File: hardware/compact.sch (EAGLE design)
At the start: 26 parts, among them SW1 SWITCH_SPDT, U1 MCP73831, U2 EDISON_CONNECTOR_FULLMOUNTING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, U3 EDISON_CONNECTOR_FULLHEADER

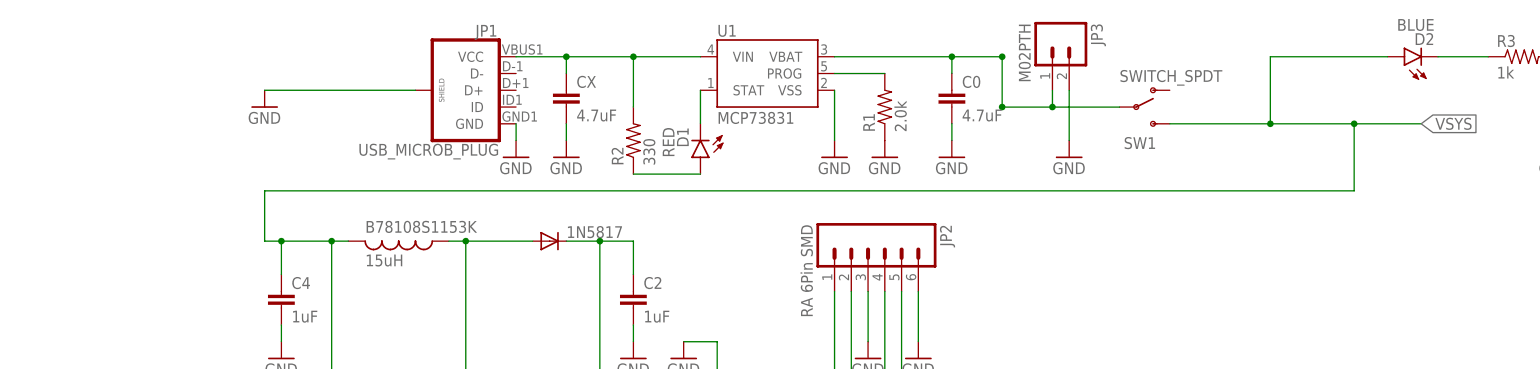
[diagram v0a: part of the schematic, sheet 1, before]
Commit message: add USB data lines, use 1.8v line, not vcc, for Max3218, DRC fixes
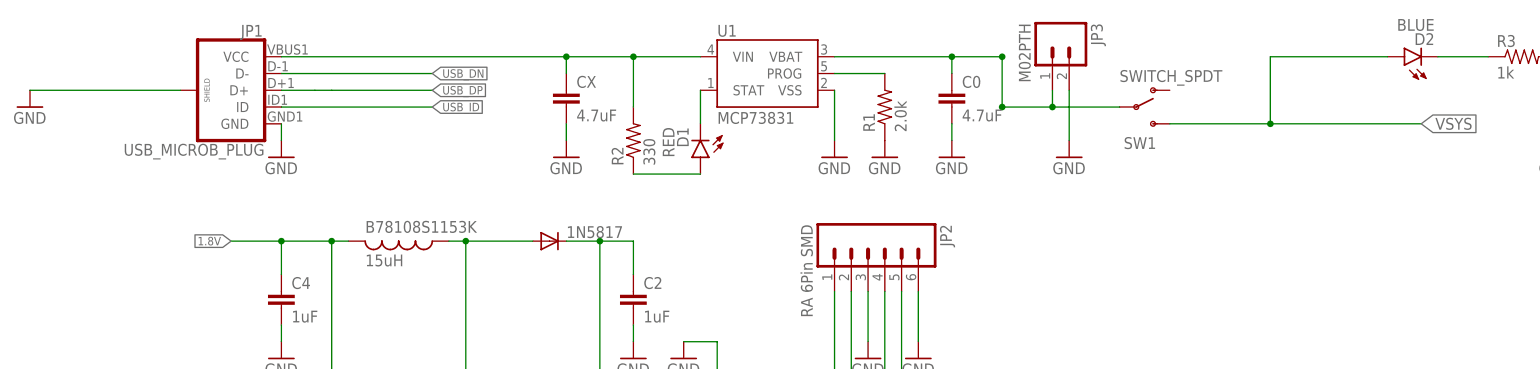
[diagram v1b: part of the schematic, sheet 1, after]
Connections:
- net 1.8V: now also B78108S1153K.2, C4.1, MAX3218.4, MAX3218.6
- net USB_DN: now also JP1.D-
- net USB_DP: now also JP1.D+
- net USB_ID: now also JP1.ID
- net VSYS: no longer B78108S1153K.2, C4.1, MAX3218.4, MAX3218.6
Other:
- moved on the sheet: JP1
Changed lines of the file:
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@@
 <instance part="FID1" gate="G$1" x="246.38" y="25.4"/>
 <instance part="FID2" gate="G$1" x="241.3" y="25.4"/>
-<instance part="JP1" gate="G$1" x="66.04" y="172.72" rot="MR0"/>
-<instance part="GND1" gate="1" x="73.66" y="162.56"/>
-<instance part="GND2" gate="1" x="35.56" y="170.18"/>
+<instance part="JP1" gate="G$1" x="30.48" y="172.72" rot="MR0"/>
+<instance part="GND1" gate="1" x="38.1" y="162.56"/>
+<instance part="GND2" gate="1" x="0" y="170.18"/>
 <instance part="CX" gate="G$1" x="81.28" y="170.18"/>
 <instance part="SW1" gate="G$1" x="167.64" y="170.18"/>
@@
 <pinref part="GND2" gate="1" pin="GND"/>
 <pinref part="JP1" gate="G$1" pin="SHIELD"/>
-<wire x1="35.56" y1="172.72" x2="58.42" y2="172.72" width="0.1524" layer="91"/>
+<wire x1="0" y1="172.72" x2="22.86" y2="172.72" width="0.1524" layer="91"/>
 </segment>
 <segment>
 <pinref part="JP1" gate="G$1" pin="GND"/>
 <pinref part="GND1" gate="1" pin="GND"/>
-<wire x1="73.66" y1="167.64" x2="73.66" y2="165.1" width="0.1524" layer="91"/>
+<wire x1="38.1" y1="167.64" x2="38.1" y2="165.1" width="0.1524" layer="91"/>
 </segment>
 <segment>
@@
 <pinref part="JP1" gate="G$1" pin="VCC"/>
 <pinref part="U1" gate="G$1" pin="VIN"/>
-<wire x1="73.66" y1="177.8" x2="81.28" y2="177.8" width="0.1524" layer="91"/>
+<wire x1="38.1" y1="177.8" x2="81.28" y2="177.8" width="0.1524" layer="91"/>
 <pinref part="CX" gate="G$1" pin="1"/>
 <wire x1="81.28" y1="177.8" x2="91.44" y2="177.8" width="0.1524" layer="91"/>
@@
 <wire x1="172.72" y1="167.64" x2="187.96" y2="167.64" width="0.1524" layer="91"/>
 <label x="210.82" y="167.64" size="1.778" layer="95" xref="yes"/>
-<wire x1="187.96" y1="167.64" x2="200.66" y2="167.64" width="0.1524" layer="91"/>
-<wire x1="200.66" y1="167.64" x2="210.82" y2="167.64" width="0.1524" layer="91"/>
+<wire x1="187.96" y1="167.64" x2="210.82" y2="167.64" width="0.1524" layer="91"/>
 <wire x1="187.96" y1="177.8" x2="187.96" y2="167.64" width="0.1524" layer="91"/>
 <junction x="187.96" y="167.64"/>
-<junction x="200.66" y="167.64"/>
-<wire x1="200.66" y1="167.64" x2="200.66" y2="157.48" width="0.1524" layer="91"/>
-<wire x1="200.66" y1="157.48" x2="35.56" y2="157.48" width="0.1524" layer="91"/>
-<wire x1="35.56" y1="157.48" x2="35.56" y2="149.86" width="0.1524" layer="91"/>
-<wire x1="35.56" y1="149.86" x2="38.1" y2="149.86" width="0.1524" layer="91"/>
-<junction x="38.1" y="149.86"/>
-<wire x1="38.1" y1="149.86" x2="38.1" y2="144.78" width="0.1524" layer="91"/>
-<wire x1="38.1" y1="149.86" x2="45.72" y2="149.86" width="0.1524" layer="91"/>
-<junction x="45.72" y="149.86"/>
-<pinref part="C4" gate="G$1" pin="1"/>
-<pinref part="MAX3218" gate="G$1" pin="6"/>
-<wire x1="58.42" y1="111.76" x2="45.72" y2="111.76" width="0.1524" layer="91"/>
-<wire x1="45.72" y1="111.76" x2="45.72" y2="116.84" width="0.1524" layer="91"/>
-<pinref part="B78108S1153K" gate="G$1" pin="2"/>
-<wire x1="45.72" y1="116.84" x2="45.72" y2="149.86" width="0.1524" layer="91"/>
-<wire x1="48.26" y1="149.86" x2="45.72" y2="149.86" width="0.1524" layer="91"/>
-<junction x="45.72" y="116.84"/>
-<pinref part="MAX3218" gate="G$1" pin="4"/>
-<wire x1="58.42" y1="116.84" x2="45.72" y2="116.84" width="0.1524" layer="91"/>
 <pinref part="D2" gate="G$1" pin="A"/>
 <wire x1="187.96" y1="177.8" x2="205.74" y2="177.8" width="0.1524" layer="91"/>
@@
 </segment>
 </net>
+<net name="1.8V" class="0">
+<segment>
+<label x="30.48" y="149.86" size="1.27" layer="95" rot="R180" xref="yes"/>
+<pinref part="C4" gate="G$1" pin="1"/>
+<junction x="38.1" y="149.86"/>
+<wire x1="38.1" y1="149.86" x2="38.1" y2="144.78" width="0.1524" layer="91"/>
+<wire x1="38.1" y1="149.86" x2="45.72" y2="149.86" width="0.1524" layer="91"/>
+<junction x="45.72" y="149.86"/>
+<pinref part="B78108S1153K" gate="G$1" pin="2"/>
+<wire x1="48.26" y1="149.86" x2="45.72" y2="149.86" width="0.1524" layer="91"/>
+<wire x1="45.72" y1="116.84" x2="45.72" y2="149.86" width="0.1524" layer="91"/>
+<junction x="45.72" y="116.84"/>
+<pinref part="MAX3218" gate="G$1" pin="4"/>
+<wire x1="58.42" y1="116.84" x2="45.72" y2="116.84" width="0.1524" layer="91"/>
+<pinref part="MAX3218" gate="G$1" pin="6"/>
+<wire x1="58.42" y1="111.76" x2="45.72" y2="111.76" width="0.1524" layer="91"/>
+<wire x1="45.72" y1="111.76" x2="45.72" y2="116.84" width="0.1524" layer="91"/>
+<wire x1="30.48" y1="149.86" x2="38.1" y2="149.86" width="0.1524" layer="91"/>
+</segment>
+</net>
+<net name="USB_DN" class="0">
+<segment>
+<label x="60.96" y="175.26" size="1.27" layer="95" xref="yes"/>
+<pinref part="JP1" gate="G$1" pin="D-"/>
+<wire x1="60.96" y1="175.26" x2="38.1" y2="175.26" width="0.1524" layer="91"/>
+</segment>
+</net>
+<net name="USB_DP" class="0">
+<segment>
+<label x="60.96" y="172.72" size="1.27" layer="95" xref="yes"/>
+<pinref part="JP1" gate="G$1" pin="D+"/>
+<wire x1="38.1" y1="172.72" x2="43.18" y2="172.72" width="0.1524" layer="91"/>
+<wire x1="43.18" y1="172.72" x2="45.72" y2="172.72" width="0.1524" layer="91"/>
+<wire x1="60.96" y1="172.72" x2="45.72" y2="172.72" width="0.1524" layer="91"/>
+</segment>
+</net>
+<net name="USB_ID" class="0">
+<segment>
+<label x="60.96" y="170.18" size="1.27" layer="95" xref="yes"/>
+<pinref part="JP1" gate="G$1" pin="ID"/>
+<wire x1="38.1" y1="170.18" x2="60.96" y2="170.18" width="0.1524" layer="91"/>
+</segment>
+</net>

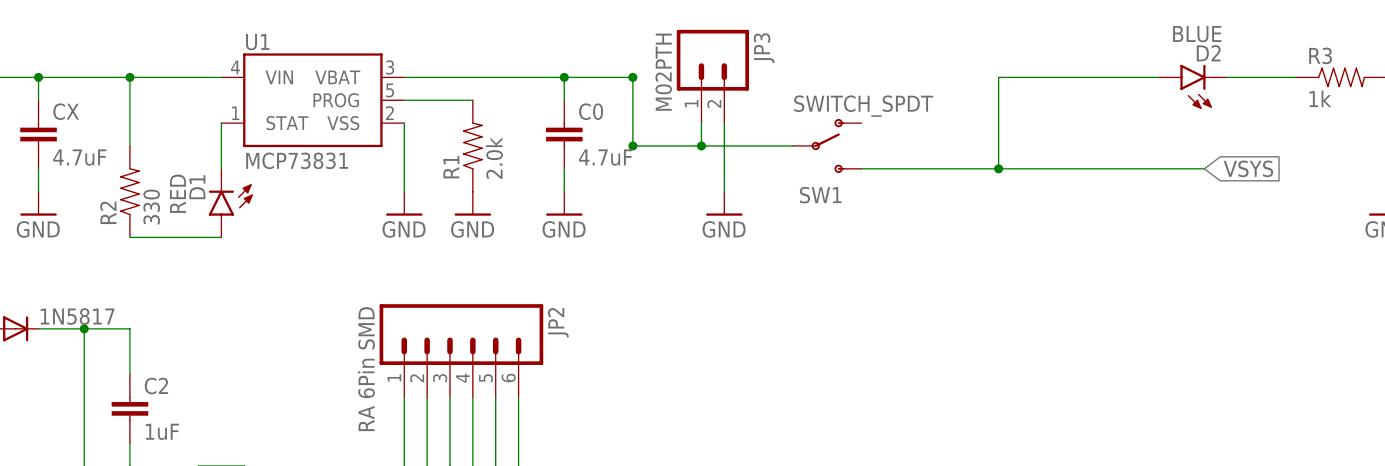
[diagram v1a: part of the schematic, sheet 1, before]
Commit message: Update readme, board routing fixes, change LED names to functions vice colors
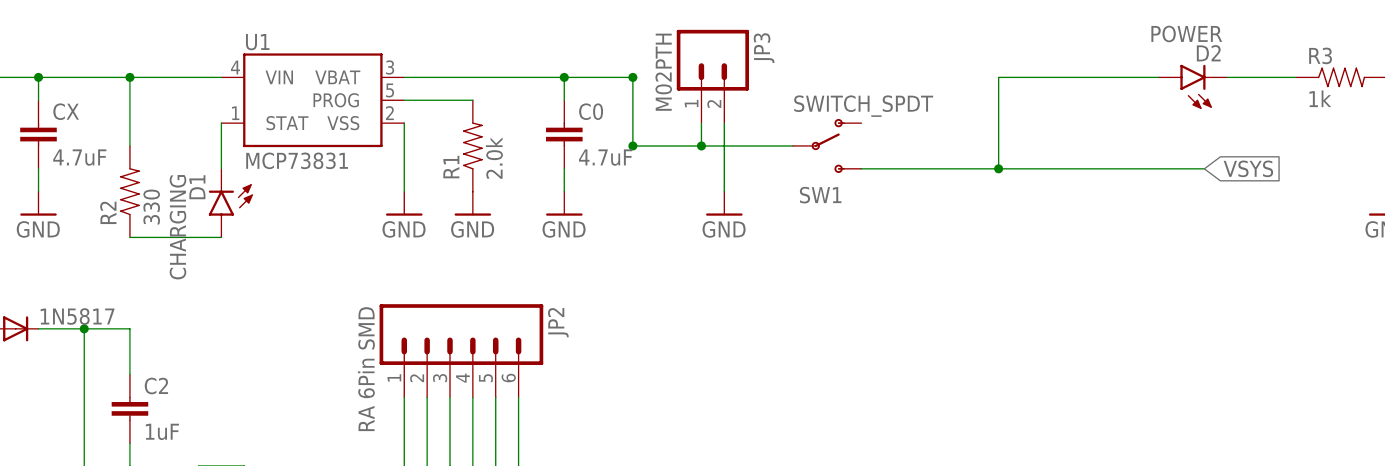
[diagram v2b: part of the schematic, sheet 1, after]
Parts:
- D1: value RED -> CHARGING
- D2: value BLUE -> POWER
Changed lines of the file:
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@@
 <part name="GND6" library="SparkFun-Aesthetics" deviceset="GND" device=""/>
 <part name="GND7" library="SparkFun-Aesthetics" deviceset="GND" device=""/>
-<part name="D1" library="SparkFun-LED" deviceset="LED-RED" device="0603" value="RED"/>
+<part name="D1" library="SparkFun-LED" deviceset="LED-RED" device="0603" value="CHARGING"/>
 <part name="C0" library="SparkFun-Capacitors" deviceset="4.7UF-6.3V-10%(0603)" device="0603" value="4.7uF"/>
 <part name="GND8" library="SparkFun-Aesthetics" deviceset="GND" device=""/>
 <part name="GND10" library="SparkFun-Aesthetics" deviceset="GND" device=""/>
-<part name="D2" library="SparkFun-LED" deviceset="LED-BLUE" device="0603" value="BLUE"/>
+<part name="D2" library="SparkFun-LED" deviceset="LED-BLUE" device="0603" value="POWER"/>
 <part name="R3" library="SparkFun-Resistors" deviceset="1KOHM1/10W1%(0603)" device="" value="1k"/>
 <part name="GND9" library="SparkFun-Aesthetics" deviceset="GND" device=""/>
